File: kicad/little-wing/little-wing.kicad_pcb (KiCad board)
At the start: 4 copper layers, 16.1 x 51.3 mm, 49 parts, among them J1 HRO_TYPE-C-31-M-14, J2 Battery, J3 rgb, J4 columns, J5 Conn_01x10, J6 rows, J7 sensor, Q1 AO3401A, Q2 2N7002, SW1 Battery, SW2 Reset, U1 BQ24075, U2 nRF52840_E73-2G4M08S1C, Y1 32.768 KHz

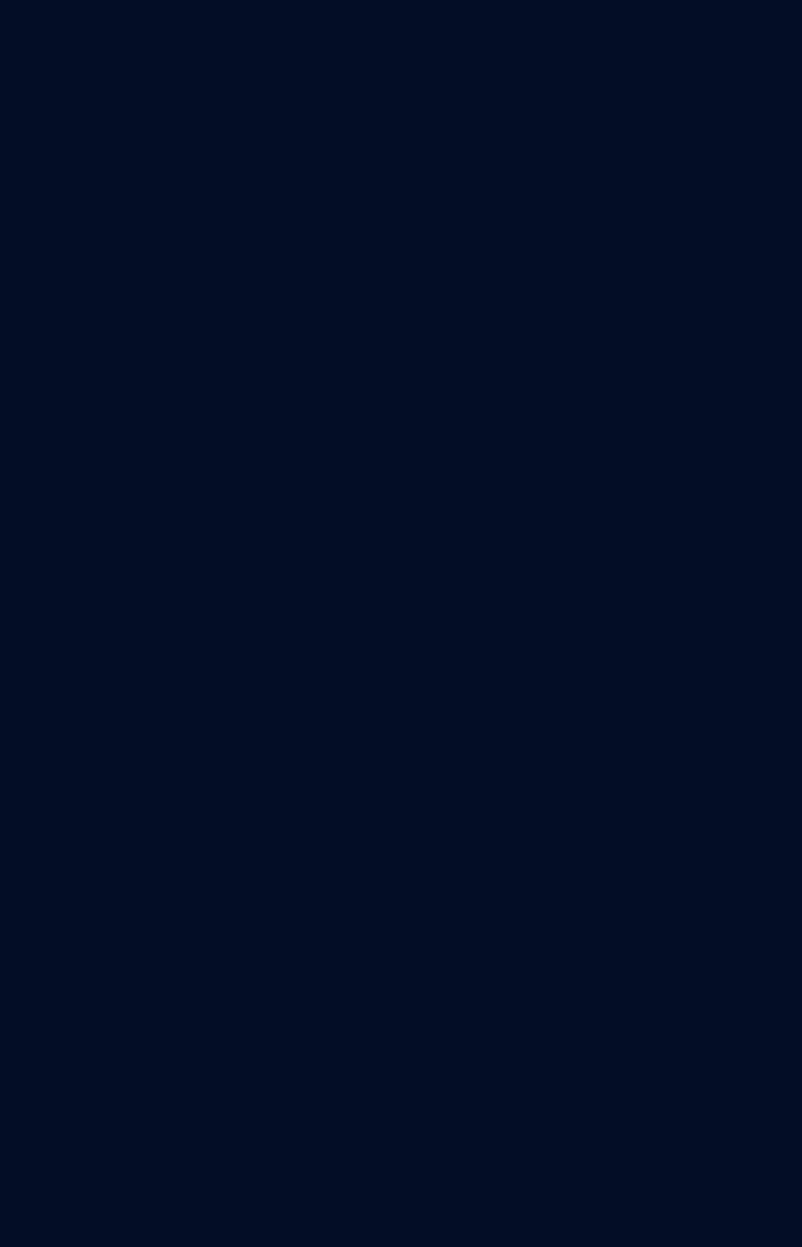
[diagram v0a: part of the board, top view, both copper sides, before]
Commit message: Copying over the reference PCB stacks
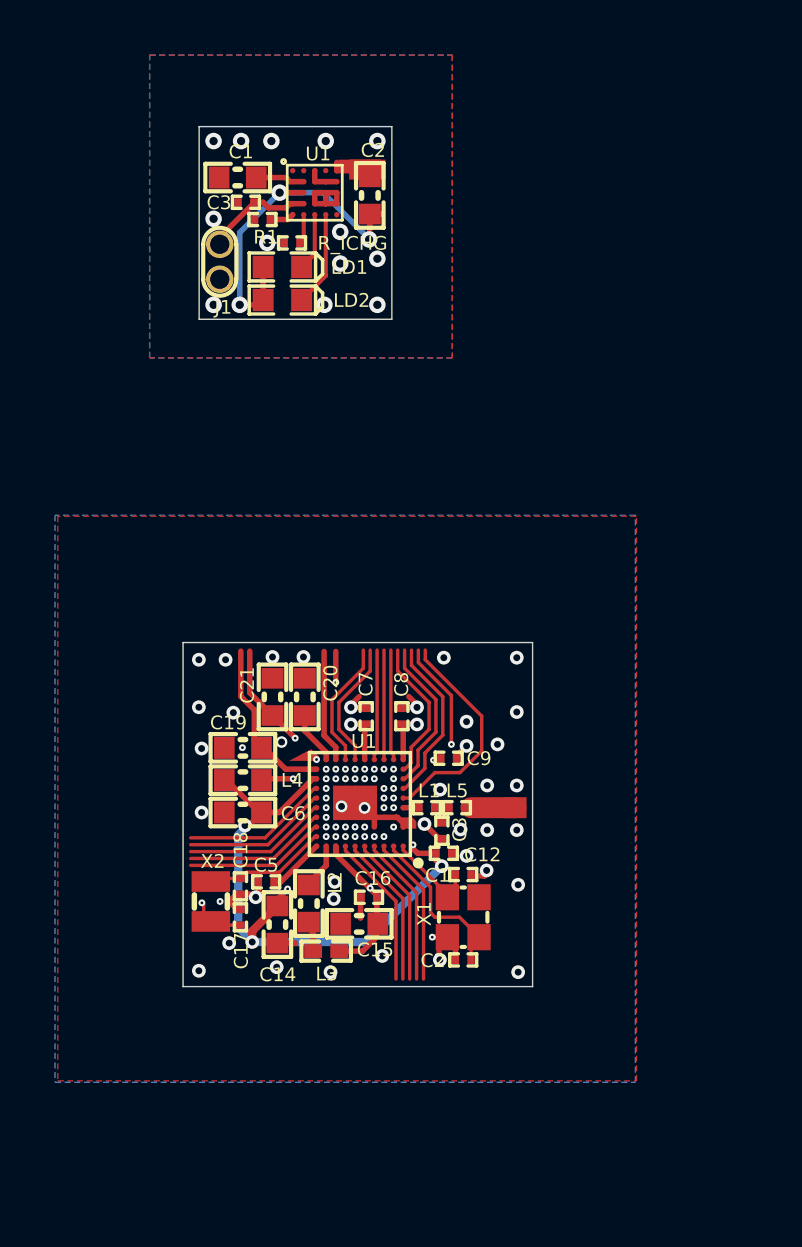
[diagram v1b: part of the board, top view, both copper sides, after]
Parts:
- added C1: 12pF, Capacitors$:CAPC0603X03L_C, F.Cu at (88.8, 80.1)
- added C1: 2.2µF, Capacitors$:CAPC1608X06L, F.Cu at (80.6, 54.7)
- added C12: 100nF, Passive:CAPC0603X03L_C, F.Cu at (88.1, 79.3)
- added C14: 1.0µF, Passive:CAPC1608X06L, F.Cu at (82.0, 81.9)
- added C15: 1.0µF, Passive:CAPC1608X06L, F.Cu at (85.0, 81.8)
- added C16: 47nF, Passive:CAPC0603X03L_C, F.Cu at (85.4, 80.9)
- added C17: 12pF, Capacitors$:CAPC0603X03L_C, F.Cu at (80.7, 81.6)
- added C18: 12pF, Capacitors$:CAPC0603X03L_C, F.Cu at (80.7, 80.5)
- added C19: 4.7µF, Passive:CAPC1608X06L, F.Cu at (80.8, 75.4)
- added C2: 22µF, Capacitors$:CAPC1608X06L, F.Cu at (85.4, 55.4)
- added C2: 12pF, Capacitors$:CAPC0603X03L_C, F.Cu at (88.8, 83.2)
- added C20: 4.7µF, Passive:CAPC1608X06L, F.Cu at (83.0, 73.6)
- added C21: 4.7µF, Passive:CAPC1608X06L, F.Cu at (81.9, 73.6)
- added C3: 1.0µF, Parts$:CAPC0603X03L_C, F.Cu at (80.9, 55.6)
- added C3: 1.0pF, Capacitors$:CAPC0603X03L_C, F.Cu at (88.0, 78.5)
- added C5: 100nF, Capacitors$:CAPC0603X03L_C, F.Cu at (81.6, 80.3)
- added C6: 4.7µF, Passive:CAPC1608X06L, F.Cu at (80.8, 77.8)
- added C7: 100nF, Capacitors$:CAPC0603X03L_C, F.Cu at (85.3, 74.3)
- added C8: 100nF, Capacitors$:CAPC0603X03L_C, F.Cu at (86.6, 74.3)
- added C9: 820pF, Capacitors$:CAPC0603X03L_C, F.Cu at (88.3, 75.8)
- added J1: Battery pack, Batteries$:TP_2x1mm_TH, F.Cu at (79.9, 57.8)
- added L1: 3.9nH, Inductors$:INDC0603X03L_C, F.Cu at (87.5, 77.6)
- added L2: 10µH, 0603:INDC1608X06L, F.Cu at (83.2, 81.1)
- added L3: 15nH, 0402:INDC1005X04L, F.Cu at (83.8, 82.8)
- added L4: 10µH, Passive:INDC1608X06L, F.Cu at (80.8, 76.6)
- added L5: 4.7nH, Passive:INDC0603X03L_C, F.Cu at (88.6, 77.6)
- added LD1: L0603R, pcblib:LED_0603_R, F.Cu at (82.2, 58.0)
- added LD2: L0603G, pcblib:LED_0603_G, F.Cu at (82.2, 59.2)
- added R1: 10k, RESC0603X03L_C:RESC0603X03L_C, F.Cu at (81.5, 56.3)
- added R_ICHG: 4k7, Passive:RESC0603X03L_C, F.Cu at (82.6, 57.1)
- added U1: nPM1100-CAAx, nRF Devices$:BGA25C40P5X5_200X200X50, F.Cu at (83.4, 55.3)
- added U1: nRF52840_CKAA, nRF Devices$:BGA94C35P10X10_352X356X50, F.Cu at (85.0, 77.4)
- added X1: 32MHz, Crystal_Osc$:BT-XTAL_2016, F.Cu at (88.8, 81.6)
- added X2: 32.768kHz, Crystal_Osc$:XTAL_2012, F.Cu at (79.6, 81.0)
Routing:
- net VDD_NRF: track 0.00 -> 37.7 mm, vias 0 -> 9
- net GND: track 65.1 -> 84.5 mm, vias 1 -> 56
- net P1.03: track 0.00 -> 13.4 mm, vias 0 -> 2
- net VOUT: track 0.00 -> 13.1 mm, vias 0 -> 3
- net P1.06: track 0.00 -> 12.6 mm, vias 0 -> 2
- net P1.02: track 0.00 -> 11.0 mm, vias 0 -> 2
- net DEC4_6: track 0.00 -> 9.88 mm, vias 0 -> 2
- net P0.24: track 0.00 -> 9.56 mm, vias 0 -> 2
- net P0.23: track 0.00 -> 9.47 mm, vias 0 -> 2
- net P0.16: track 0.00 -> 8.49 mm, vias 0 -> 2
- net P1.12: track 0.00 -> 8.29 mm, vias 0 -> 2
- net P1.15: track 0.00 -> 8.28 mm, vias 0 -> 2
- net P0.13: track 0.00 -> 8.12 mm, vias 0 -> 2
- net P0.09/NFC1: track 0.00 -> 8.07 mm
- net P0.11: track 0.00 -> 7.57 mm, vias 0 -> 2
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- added copper zone on B.Cu, net GND
- added copper zone on F.Cu, net GND
- added copper zone on In1.Cu, net GND
- added copper zone on In2.Cu, net GND
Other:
- board size 16.1 x 51.3 mm -> 79.4 x 55.9 mm
- rule pad_to_mask_clearance: 0 -> 0.0762

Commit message: Tidying up the mess a little bit
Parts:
- removed the C1 at (154.9, 69.6)
- removed C11: 12p, Capacitor_SMD:C_0402_1005Metric
- removed the C2 at (150.8, 72.5)
- removed the C3 at (148.1, 70.7)
- removed C4: 1u, Capacitor_SMD:C_0402_1005Metric
- removed the C5 at (147.4, 74.9)
- removed the C6 at (148.4, 74.9)
- removed the C7 at (154.3, 91.8)
- removed the C8 at (149.5, 87.3)
- removed the C9 at (155.9, 79.4)
- removed the J1 at (150.0, 60.0)
- removed the L1 at (147.4, 79.4)
- removed LED1: orange, LED_SMD:LED_0402_1005Metric
- removed the R1 at (151.8, 66.5)
- removed R3: 10k, Resistor_SMD:R_0402_1005Metric
- removed R4, R6: 1k5, Resistor_SMD:R_0402_1005Metric
- removed R5: 47k, Resistor_SMD:R_0402_1005Metric
- removed R7: 3k9, Resistor_SMD:R_0402_1005Metric
- removed R_ICHG: 4k7, Passive:RESC0603X03L_C
- removed the U1 at (150.7, 69.8)
- removed U2: nRF52840_E73-2G4M08S1C, E73-2G4M08S1C Model:E73-2G4M08S1C
- removed Y1: 32.768 KHz, Crystal:Crystal_SMD_2012-2Pin_2.0x1.2mm
- C1: value 12pF -> 4.7µF
- C1: value 2.2µF -> 4.7µF
- C12: value 100nF -> 1.0µF
- C14, C15: value 1.0µF -> 100nF
- C16: value 47nF -> 820pF
- C17: value 12pF -> 100nF
- C19: value 4.7µF -> 12pF
- C2: value 22µF -> 12pF
- C20: value 4.7µF -> 1.0pF
- C21: value 4.7µF -> 2.2µF
- C3: value 1.0µF -> 12pF
- C3: value 1.0pF -> 12pF
- C7: value 100nF -> 560pF/680pF; footprint Capacitors$:CAPC0603X03L_C -> Capacitor_SMD:C_0603_1608Metric_Pad1.08x0.95mm_HandSolder
- C8: value 100nF -> 1uF; footprint Capacitors$:CAPC0603X03L_C -> Capacitor_SMD:C_0603_1608Metric_Pad1.08x0.95mm_HandSolder
- C9: value 820pF -> 1.0µF
- FB1, FB2: footprint Resistor_SMD:R_0603_1608Metric -> Resistor_SMD:R_0805_2012Metric_Pad1.20x1.40mm_HandSolder
- J1: value Battery pack -> HRO_TYPE-C-31-M-14; footprint Batteries$:TP_2x1mm_TH -> Connector_USB:USB_C_Receptacle_HRO_TYPE-C-31-M-12
- J5: footprint Hirose FH34SRJ-10S-0.5SH:CONN10x1_FH34SRJ-10S-0.5SH50_HIR -> Connector_FFC-FPC:Hirose_FH12-10S-0.5SH_1x10-1MP_P0.50mm_Horizontal
- L1: value 3.9nH -> 10µH
- L2: value 10µH -> 15nH
- L3: value 15nH -> 10µH
- L4: value 10µH -> 3.9nH
- R1: value 10k -> 5k1; footprint RESC0603X03L_C:RESC0603X03L_C -> Resistor_SMD:R_0402_1005Metric
- R12, R13, R9: footprint Resistor_SMD:R_0402_1005Metric -> Resistor_SMD:R_0603_1608Metric_Pad0.98x0.95mm_HandSolder
- SW2 (x2): footprint Button_Switch_SMD:SW_SPST_B3U-3000P-B -> Button_Switch_SMD:SW_SPST_B3U-1000P
- U1: value nPM1100-CAAx -> nRF52840_CKAA
- X1: value 32MHz -> 32.768kHz
- X2: value 32.768kHz -> 32MHz
- moved C21 75.1 mm to (154.3, 93.3), turned to 0 degrees
- moved C20 74.3 mm to (154.3, 94.5), turned to 0 degrees
- moved R2 74.0 mm to (99.9, 123.5)
- moved C19 73.6 mm to (152.5, 92.3), turned to 90 degrees
- moved R13 73.4 mm to (86.4, 122.3), turned to 0 degrees
- moved L4 72.2 mm to (151.3, 92.3), turned to -90 degrees
- moved C7 72.0 mm to (153.6, 96.7), turned to 0 degrees
- moved R9 71.8 mm to (86.4, 117.2), turned to 0 degrees
- moved C8 71.1 mm to (153.6, 98.0), turned to 0 degrees
- moved C6 70.8 mm to (150.1, 92.3), turned to 90 degrees
- moved J1 70.1 mm to (150.0, 60.0), turned to 180 degrees
- moved R12 69.4 mm to (86.4, 119.8), turned to 0 degrees
- moved R17 69.2 mm to (99.9, 117.5), turned to 0 degrees
- moved C9 68.2 mm to (152.1, 99.7), turned to -90 degrees
- moved U1 68.2 mm to (150.5, 96.5), turned to 90 degrees
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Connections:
- net D+ renamed /Main Module/MCU/D+
- net D- renamed /Main Module/MCU/D-
- net DEC1 renamed /Main Module/MCU/DEC1
- net P0.02/AIN0 renamed /Main Module/MCU/P0.02/AIN0
- net P0.04/AIN2 renamed /Main Module/MCU/P0.04/AIN2
- net P0.05/AIN3 renamed /Main Module/MCU/P0.05/AIN3
- net P0.06 renamed /Main Module/MCU/P0.06
- net P0.07 renamed /Main Module/MCU/P0.07
- net P0.08 renamed /Main Module/MCU/P0.08
- net P0.09/NFC1 renamed /Main Module/MCU/P0.09/NFC1
- net P0.11 renamed /Main Module/MCU/P0.11
- net P0.12 renamed /Main Module/MCU/P0.12
- net P0.13 renamed /Main Module/MCU/P0.13
- net P0.14 renamed /Main Module/MCU/P0.14
- net P0.15 renamed /Main Module/MCU/P0.15
- net P0.16 renamed /Main Module/MCU/P0.16
- net P0.17 renamed /Main Module/MCU/P0.17
- net P0.19 renamed /Main Module/MCU/P0.19
- net P0.20 renamed /Main Module/MCU/P0.20
- net P0.21 renamed /Main Module/MCU/P0.21
- net P0.22 renamed /Main Module/MCU/P0.22
- net P0.23 renamed /Main Module/MCU/P0.23
- net P0.24 renamed /Main Module/MCU/P0.24
- net P0.25 renamed /Main Module/MCU/P0.25
- net P0.26 renamed /Main Module/MCU/P0.26
- net P0.27 renamed /Main Module/MCU/P0.27
- net P0.28/AIN4 renamed /Main Module/MCU/P0.28/AIN4
- net P0.29/AIN5 renamed /Main Module/MCU/P0.29/AIN5
- net P0.30/AIN6 renamed /Main Module/MCU/P0.30/AIN6
- net P0.31/AIN7 renamed /Main Module/MCU/P0.31/AIN7
- net P1.00 renamed /Main Module/MCU/P1.00
- net P1.01 renamed /Main Module/MCU/P1.01
- net P1.02 renamed /Main Module/MCU/P1.02
- net P1.03 renamed /Main Module/MCU/P1.03
- net P1.04 renamed /Main Module/MCU/P1.04
- net P1.05 renamed /Main Module/MCU/P1.05
- net P1.07 renamed /Main Module/MCU/P1.07
- net P1.08 renamed /Main Module/MCU/P1.08
- net P1.09 renamed /Main Module/MCU/P1.09
- net P1.15 renamed /Main Module/MCU/P1.15
- net RF renamed /Main Module/MCU/RF
- net SWDCLK renamed /Main Module/MCU/SWDCLK
- net SWDIO renamed /Main Module/MCU/SWDIO
- C1 pad 1: XC1 -> VDD_nRF
- C1 pad 1: GND -> VDD_nRF
- C1 pad 2: VBUS -> GND
- C12 pad 1: VDD_NRF -> GND
- C12 pad 2: GND -> /Main Module/MCU/DEC4_6
- C14 pad 1: VDD_NRF -> VDD_nRF
- C15 pad 1: GND -> VDD_nRF
- C15 pad 2: DEC4_6 -> GND
- C16 pad 1: DEC4_6 -> Net-(U1-DEC5)
- C17 pad 1: P0.00/XL1 -> VDD_nRF
- C18 pad 1: P0.01/XL2 -> /Main Module/MCU/XC2
- C19 pad 1: VDDH -> /Main Module/MCU/XC1
- C2 pad 1: GND -> /Main Module/MCU/P0.00/XL1
- C2 pad 2: VOUT -> GND
- C2 pad 1: XC2 -> /Main Module/MCU/P0.00/XL1
- C20 pad 1: NetC20_1 -> GND
- C20 pad 2: GND -> Net-(C20-Pad2)
- C21 pad 1: VBUS -> GND
- C21 pad 2: GND -> VBUS
- C3 pad 1: GND -> /Main Module/MCU/P0.01/XL2 (x2)
- C3 pad 2: VBAT -> GND
- C3 pad 2: NetC3_2 -> GND
- C6 pad 1: VDD_NRF -> Net-(U1-DECUSB)
- C7 pad 1: VDD_NRF -> Net-(J5-Pin_5)
- C8 pad 1: VDD_NRF -> VDD
- C9 pad 1: NetC9_1 -> VDD_nRF
- J7 pad 1: VDD -> +3.3V
- L1 pad 1: NetL1_1 -> VDD_nRF
- L1 pad 2: NetC3_2 -> Net-(U1-DCCH)
- L2 pad 1: NetL2_1 -> /Main Module/MCU/DEC4_6
- L2 pad 2: NetL2_2 -> Net-(L2-Pad2)
- L3 pad 1: DEC4_6 -> Net-(L2-Pad2)
- L3 pad 2: NetL2_1 -> Net-(U1-DCC)
- L4 pad 1: VDD_NRF -> Net-(U1-ANT)
- L4 pad 2: NetL4_2 -> Net-(C20-Pad2)
- L5 pad 1: NetC3_2 -> Net-(C20-Pad2)
- LD1 pad 1: ERR -> /Main Module/PSU/ERR
- LD2 pad 1: CHG -> /Main Module/PSU/CHG
- R1 pad 1: NetR1_1 -> GND
- R1 pad 2: GND -> Net-(J1-CC1)
- SW1 pad 2: +BATT -> VBAT (x2)
- U1 pad A1: GND -> /Main Module/MCU/XC1
- U1 pad A2: (no net) -> /Main Module/MCU/XC2
- U1 pad A3: NetU1_A3 -> /Main Module/MCU/P1.11
- U1 pad A4: (no net) -> /Main Module/MCU/P1.13
- U1 pad A5: GND -> /Main Module/MCU/P0.03/AIN1
- U1 pad B1: VBUS -> (no net)
- U1 pad B2: VBUS -> (no net)
- U1 pad B3: NetU1_A3 -> VDD_nRF
- U1 pad B4: NetU1_A3 -> /Main Module/MCU/P1.10
- U1 pad B5: NetU1_A3 -> /Main Module/MCU/P1.14
- U1 pad C1: VOUT -> GND
- U1 pad C2: VOUT -> /Main Module/MCU/DEC4_6
- U1 pad C3: GND -> (no net)
- U1 pad C5: GND -> /Main Module/MCU/P1.12
- U1 pad D1: VBAT -> (no net)
- U1 pad D2: VBAT -> (no net)
- U1 pad E1: NetR1_1 -> Net-(U1-ANT)
- U1 pad E2: NetR_ICHG_2 -> /Main Module/MCU/P0.10/NFC2
- U1 pad E3: ERR -> /Main Module/MCU/P1.06
- U1 pad E4: CHG -> GND
- U1 pad A1: XC1 -> /Main Module/MCU/XC1
- U1 pad A2: XC2 -> /Main Module/MCU/XC2
- U1 pad A3: P1.11 -> /Main Module/MCU/P1.11
- U1 pad A4: P1.13 -> /Main Module/MCU/P1.13
- U1 pad A5: P0.03/AIN1 -> /Main Module/MCU/P0.03/AIN1
- U1 pad A8: DEC4_6 -> /Main Module/MCU/DEC4_6
- U1 pad A9: NetL2_2 -> Net-(U1-DCC)
- U1 pad B10: P0.01/XL2 -> /Main Module/MCU/P0.01/XL2
- U1 pad B3: VDD_NRF -> VDD_nRF
- U1 pad B4: P1.10 -> /Main Module/MCU/P1.10
- U1 pad B5: P1.14 -> /Main Module/MCU/P1.14
- U1 pad B8: VDD_NRF -> VDD_nRF
- U1 pad B9: P0.00/XL1 -> /Main Module/MCU/P0.00/XL1
- U1 pad C2: DEC4_6 -> /Main Module/MCU/DEC4_6
- U1 pad C5: P1.12 -> /Main Module/MCU/P1.12
- U1 pad E1: NetL1_1 -> Net-(U1-ANT)
- U1 pad E2: P0.10/NFC2 -> /Main Module/MCU/P0.10/NFC2
- U1 pad E3: P1.06 -> /Main Module/MCU/P1.06
- U1 pad F2: NetC9_1 -> Net-(U1-DEC5)
- U1 pad H10: VDD_NRF -> VDD_nRF
- U1 pad H9: NetL4_2 -> Net-(U1-DCCH)
- U1 pad K1: VDD_NRF -> VDD_nRF
- U1 pad K5: VDD_NRF -> VDD_nRF
- U1 pad K6: P0.18/RESET -> RST
- U1 pad K9: NetC20_1 -> Net-(U1-DECUSB)
- X1 pad 1: XC1 -> /Main Module/MCU/P0.00/XL1
- X1 pad 2: GND -> /Main Module/MCU/P0.01/XL2
- X1 pad 3: XC2 -> (no net)
- X1 pad 4: GND -> (no net)
- X2 pad 1: P0.00/XL1 -> /Main Module/MCU/XC1
- X2 pad 2: P0.01/XL2 -> unconnected-(X2-GND-Pad2)
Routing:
- net (no net): track 0.00 -> 93.0 mm, vias 0 -> 6
- net GND: track 84.5 -> 37.4 mm
- net VDD_NRF: track 37.7 -> 0.00 mm, vias 9 -> 0
- net Net-(J2-Pin_1): track 17.6 -> 0.00 mm, vias 2 -> 1
- net Net-(J3-Pin_2): track 14.7 -> 0.00 mm
- net P1.06: track 12.6 -> 0.00 mm, vias 2 -> 0
- net /Main Module/MCU/P1.06: track 0.00 -> 12.6 mm, vias 0 -> 2
- net +BATT: track 10.1 -> 0.00 mm, vias 1 -> 0
- net DEC4_6: track 9.88 -> 0.00 mm, vias 2 -> 0
- net EXTMODE: track 9.46 -> 0.00 mm
- net Net-(J5-Pin_5): track 9.46 -> 0.00 mm
- net VDDA: track 9.45 -> 0.00 mm
- net VDD: track 9.41 -> 0.00 mm
- net GNDA: track 9.04 -> 0.00 mm
- net /Main Module/MCU/P0.10/NFC2: track 0.00 -> 8.33 mm, vias 0 -> 2
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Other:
- board size 79.4 x 55.9 mm -> 58.2 x 59.5 mm

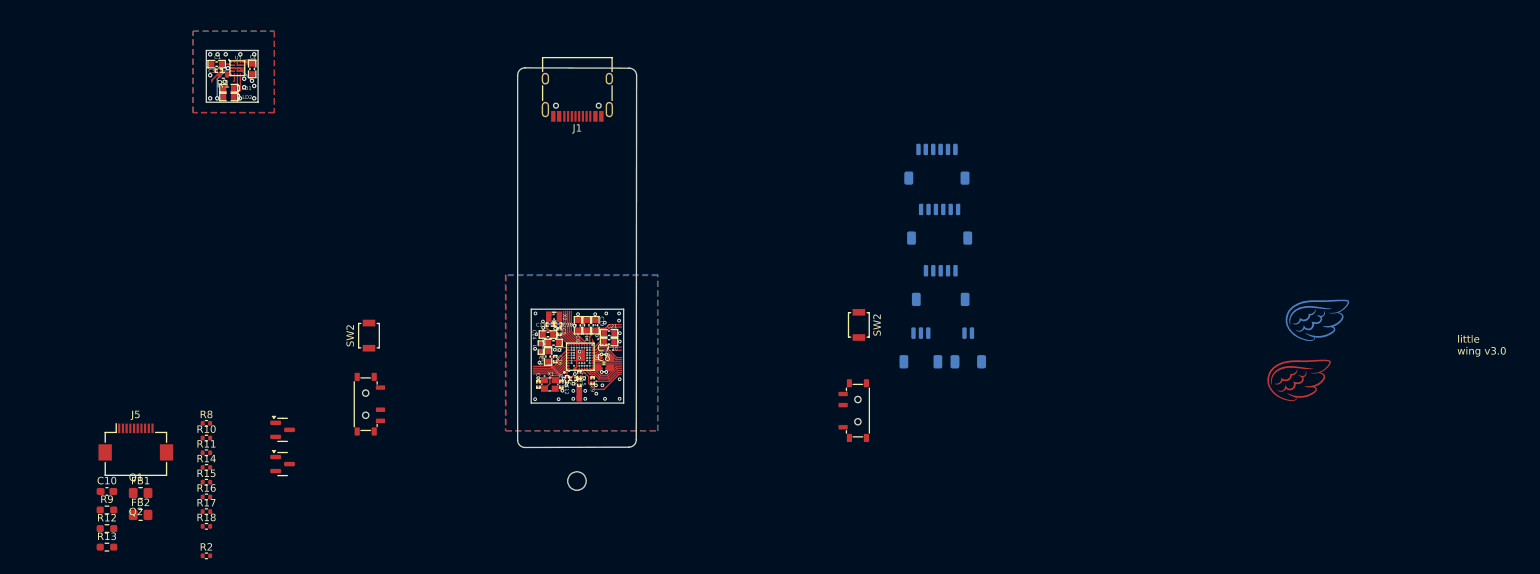
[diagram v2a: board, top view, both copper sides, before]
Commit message: Re-importing some key components
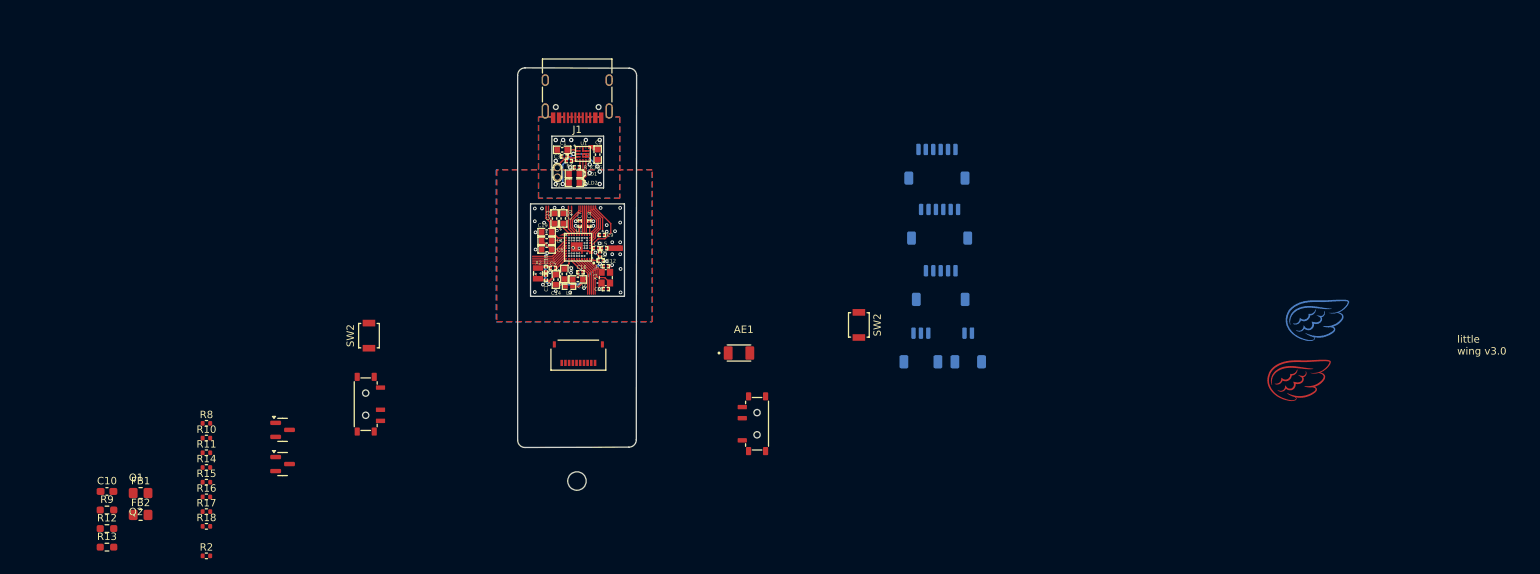
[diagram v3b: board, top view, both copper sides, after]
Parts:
- removed the C1 at (147.9, 100.3)
- removed the C1 at (101.3, 57.0)
- removed the C2 at (106.1, 57.6)
- removed the C2 at (144.8, 100.3)
- removed the C3 at (101.6, 57.9)
- removed the C3 at (149.5, 99.5)
- removed the U1 at (104.1, 57.5)
- removed the U1 at (150.5, 96.5)
- added AE1: 2450AT18A100E, JTI Antenna:ANTC3216X140N, F.Cu at (171.9, 96.0)
- added C1: 12pF, Capacitors$:CAPC0603X03L_C, F.Cu at (153.9, 84.3)
- added C1: 2.2µF, Capacitors$:CAPC1608X06L, F.Cu at (148.0, 68.5)
- added C2: 22µF, Capacitors$:CAPC1608X06L, F.Cu at (152.8, 69.2)
- added C2: 12pF, Capacitors$:CAPC0603X03L_C, F.Cu at (153.9, 87.4)
- added C3: 1.0pF, Capacitors$:CAPC0603X03L_C, F.Cu at (153.1, 82.7)
- added C3: 1.0µF, Parts$:CAPC0603X03L_C, F.Cu at (148.3, 69.4)
- added J1: Battery pack, Batteries$:TP_2x1mm_TH, F.Cu at (147.3, 71.6)
- added R_ICHG: 4k7, Passive:RESC0603X03L_C, F.Cu at (150.0, 70.9)
- added U1: nPM1100-CAAx, nRF Devices$:BGA25C40P5X5_200X200X50, F.Cu at (150.8, 69.1)
- added U1: nRF52840_CKAA, nRF Devices$:BGA94C35P10X10_352X356X50, F.Cu at (150.1, 81.7)
- C12: value 1.0µF -> 100nF
- C14, C15: value 100nF -> 1.0µF
- C16: value 820pF -> 47nF
- C17: value 100nF -> 12pF
- C19: value 12pF -> 4.7µF
- C20: value 1.0pF -> 4.7µF
- C21: value 2.2µF -> 4.7µF
- C7: value 560pF/680pF -> 100nF; footprint Capacitor_SMD:C_0603_1608Metric_Pad1.08x0.95mm_HandSolder -> Capacitors$:CAPC0603X03L_C
- C8: value 1uF -> 100nF; footprint Capacitor_SMD:C_0603_1608Metric_Pad1.08x0.95mm_HandSolder -> Capacitors$:CAPC0603X03L_C
- C9: value 1.0µF -> 820pF
- J5: footprint Connector_FFC-FPC:Hirose_FH12-10S-0.5SH_1x10-1MP_P0.50mm_Horizontal -> Hirose FH34SRJ-10S-0.5SH:CONN10x1_FH34SRJ-10S-0.5SH50_HIR
- L1: value 10µH -> 3.9nH
- L2: value 15nH -> 10µH
- L3: value 10µH -> 15nH
- L4: value 3.9nH -> 10µH
- R1: value 5k1 -> 10k; footprint Resistor_SMD:R_0402_1005Metric -> RESC0603X03L_C:RESC0603X03L_C
- X1: value 32.768kHz -> 32MHz
- X2: value 32MHz -> 32.768kHz
- moved J5 61.0 mm to (150.2, 96.3), turned to 180 degrees
- moved LD1 48.1 mm to (149.6, 71.8)
- moved LD2 48.1 mm to (149.6, 73.0)
- moved R1 48.1 mm to (148.9, 70.1)
- moved C9 19.7 mm to (153.4, 80.1), turned to 0 degrees
- moved C8 19.6 mm to (151.6, 78.5), turned to 90 degrees
- moved C7 18.5 mm to (150.4, 78.5), turned to 90 degrees
- moved L5 18.5 mm to (153.6, 81.8), turned to 0 degrees
- moved C20 17.8 mm to (148.1, 77.8), turned to 90 degrees
- moved L1 17.2 mm to (152.6, 81.8), turned to 0 degrees
- moved C21 17.2 mm to (147.0, 77.8), turned to 90 degrees
- moved C12 16.7 mm to (153.2, 83.5), turned to 0 degrees
- moved X1 16.3 mm to (153.9, 85.8), turned to -90 degrees
- moved C19 14.2 mm to (145.9, 79.7), turned to 180 degrees
- moved SW1 13.8 mm to (174.3, 105.6)
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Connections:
- net /Main Module/MCU/RF renamed RF
- C12 pad 1: GND -> VDD_NRF
- C12 pad 2: /Main Module/MCU/DEC4_6 -> GND
- C14 pad 1: VDD_nRF -> VDD_NRF
- C15 pad 1: VDD_nRF -> GND
- C15 pad 2: GND -> DEC4_6
- C16 pad 1: Net-(U1-DEC5) -> DEC4_6
- C17 pad 1: VDD_nRF -> P0.00/XL1
- C18 pad 1: /Main Module/MCU/XC2 -> P0.01/XL2
- C19 pad 1: /Main Module/MCU/XC1 -> VDDH
- C20 pad 1: GND -> NetC20_1
- C20 pad 2: Net-(C20-Pad2) -> GND
- C21 pad 1: GND -> VBUS
- C21 pad 2: VBUS -> GND
- C5 pad 1: /Main Module/MCU/DEC1 -> DEC1
- C6 pad 1: Net-(U1-DECUSB) -> VDD_NRF
- C7 pad 1: Net-(J5-Pin_5) -> VDD_NRF
- C8 pad 1: VDD -> VDD_NRF
- C9 pad 1: VDD_nRF -> NetC9_1
- L1 pad 1: VDD_nRF -> NetL1_1
- L1 pad 2: Net-(U1-DCCH) -> NetC3_2
- L2 pad 1: /Main Module/MCU/DEC4_6 -> NetL2_1
- L2 pad 2: Net-(L2-Pad2) -> NetL2_2
- L3 pad 1: Net-(L2-Pad2) -> DEC4_6
- L3 pad 2: Net-(U1-DCC) -> NetL2_1
- L4 pad 1: Net-(U1-ANT) -> VDD_NRF
- L4 pad 2: Net-(C20-Pad2) -> NetL4_2
- L5 pad 1: Net-(C20-Pad2) -> NetC3_2
- LD1 pad 1: /Main Module/PSU/ERR -> ERR
- LD2 pad 1: /Main Module/PSU/CHG -> CHG
- R1 pad 1: GND -> NetR1_1
- R1 pad 2: Net-(J1-CC1) -> GND
- X1 pad 1: /Main Module/MCU/P0.00/XL1 -> XC1
- X1 pad 2: /Main Module/MCU/P0.01/XL2 -> GND
- X1 pad 3: (no net) -> XC2
- X1 pad 4: (no net) -> GND
- X2 pad 1: /Main Module/MCU/XC1 -> P0.00/XL1
- X2 pad 2: unconnected-(X2-GND-Pad2) -> P0.01/XL2
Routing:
- net (no net): track 93.0 -> 0.00 mm, vias 6 -> 0
- net VDD_NRF: track 0.00 -> 37.7 mm, vias 0 -> 9
- net GND: track 37.4 -> 19.4 mm, vias 56 -> 57
- net P1.03: track 0.00 -> 13.4 mm, vias 0 -> 2
- net /Main Module/MCU/P1.03: track 13.4 -> 0.00 mm, vias 2 -> 0
- net /Main Module/MCU/P1.06: track 12.6 -> 0.00 mm, vias 2 -> 0
- net P1.06: track 0.00 -> 12.6 mm, vias 0 -> 2
- net /Main Module/MCU/P1.02: track 11.0 -> 0.00 mm, vias 2 -> 0
- net P1.02: track 0.00 -> 11.0 mm, vias 0 -> 2
- net DEC4_6: track 0.00 -> 9.88 mm, vias 0 -> 2
- net P0.24: track 0.00 -> 9.56 mm, vias 0 -> 2
- net /Main Module/MCU/P0.24: track 9.56 -> 0.00 mm, vias 2 -> 0
- net P0.23: track 0.00 -> 9.47 mm, vias 0 -> 2
- net /Main Module/MCU/P0.23: track 9.47 -> 0.00 mm, vias 2 -> 0
- net P0.16: track 0.00 -> 8.49 mm, vias 0 -> 2
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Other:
- board size 58.2 x 59.5 mm -> 16.1 x 57.1 mm
